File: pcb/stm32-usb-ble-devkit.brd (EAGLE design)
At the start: 90 x 50 mm, 98 parts, among them CN1 USB-MICROB-2TABS, CN2 USB-C-2.0-FEMALE, CN3 USB-C-2.0-FEMALE, Q2 AO3402, Q4 AO3401, Q6 AO3401, Q8 AO3401, U1 STM32F103-48LQFP, U2 STM32F205-64, U3 TUSB320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

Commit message: pcb: Fix STM32 VCAP pins
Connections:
- net GND: no longer U2.31, U2.47
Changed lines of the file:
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@@
 </signal>
 <signal name="GND">
-<contactref element="U1" pad="47"/>
 <contactref element="U1" pad="35"/>
 <contactref element="U1" pad="23"/>
@@
 <contactref element="C10" pad="1"/>
 <contactref element="R11" pad="1"/>
-<contactref element="U2" pad="47"/>
-<contactref element="U2" pad="31"/>
 <contactref element="C11" pad="1"/>
 <contactref element="C12" pad="1"/>

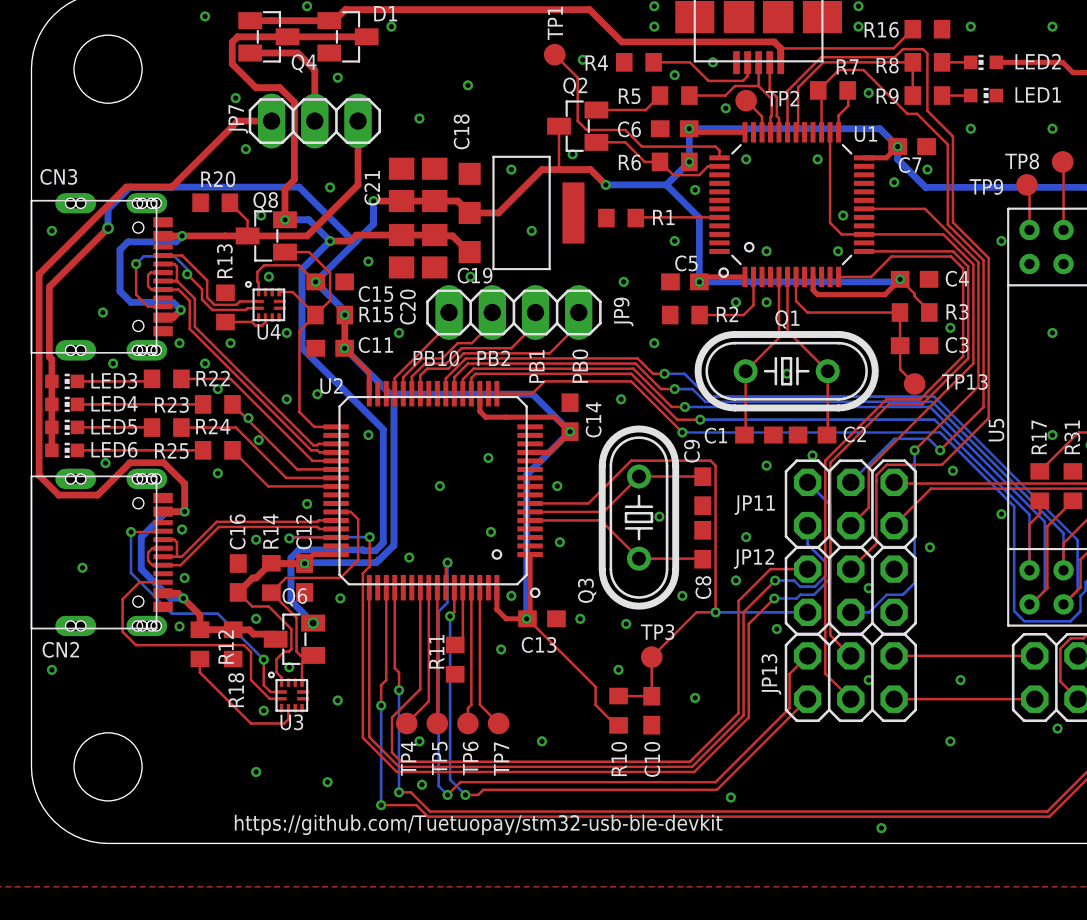
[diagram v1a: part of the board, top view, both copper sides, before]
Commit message: pcb: Misc changes following via size fix
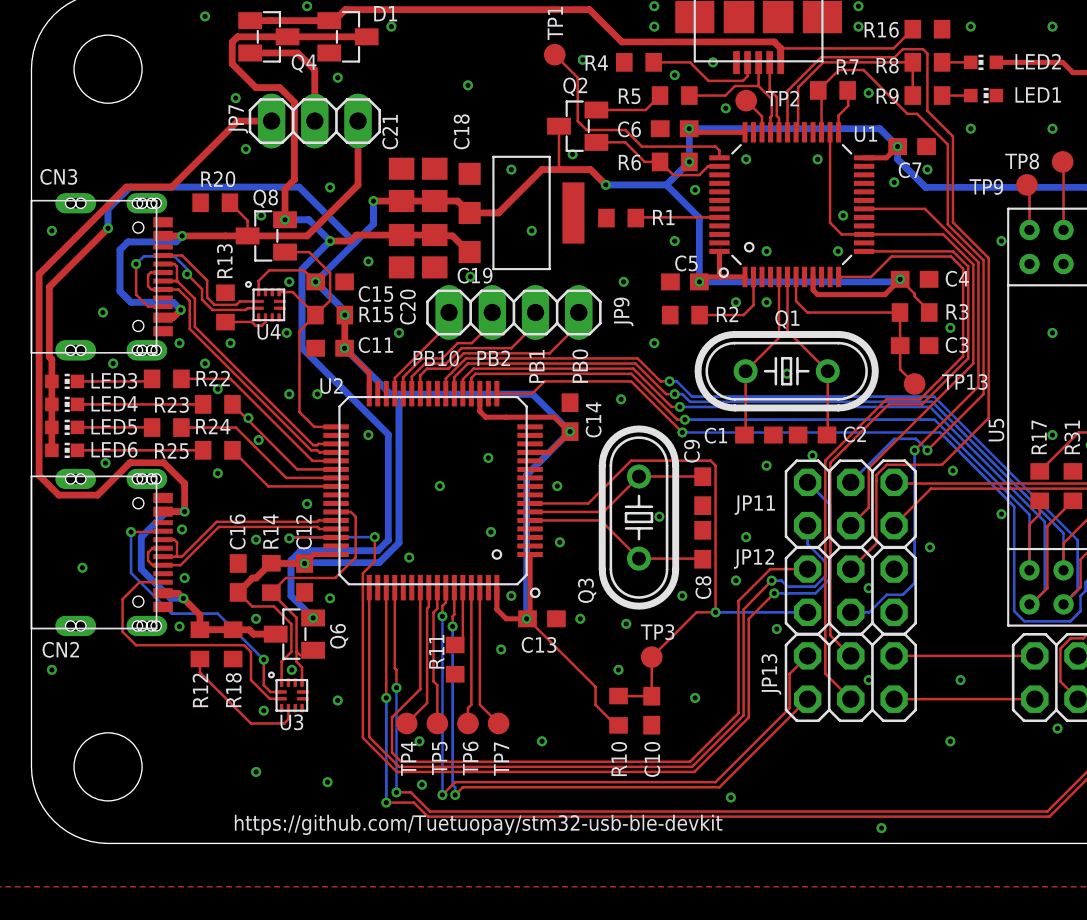
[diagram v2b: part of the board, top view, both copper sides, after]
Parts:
- moved Q6 0.30 mm to (15.4, 12.3)
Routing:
- net STM_TX: track 41.3 -> 38.3 mm
- net USB_FS_ID: track 16.8 -> 16.0 mm
- net STM_SWDIO: track 61.9 -> 62.5 mm
- net UART_STM2NRF: track 61.1 -> 60.6 mm

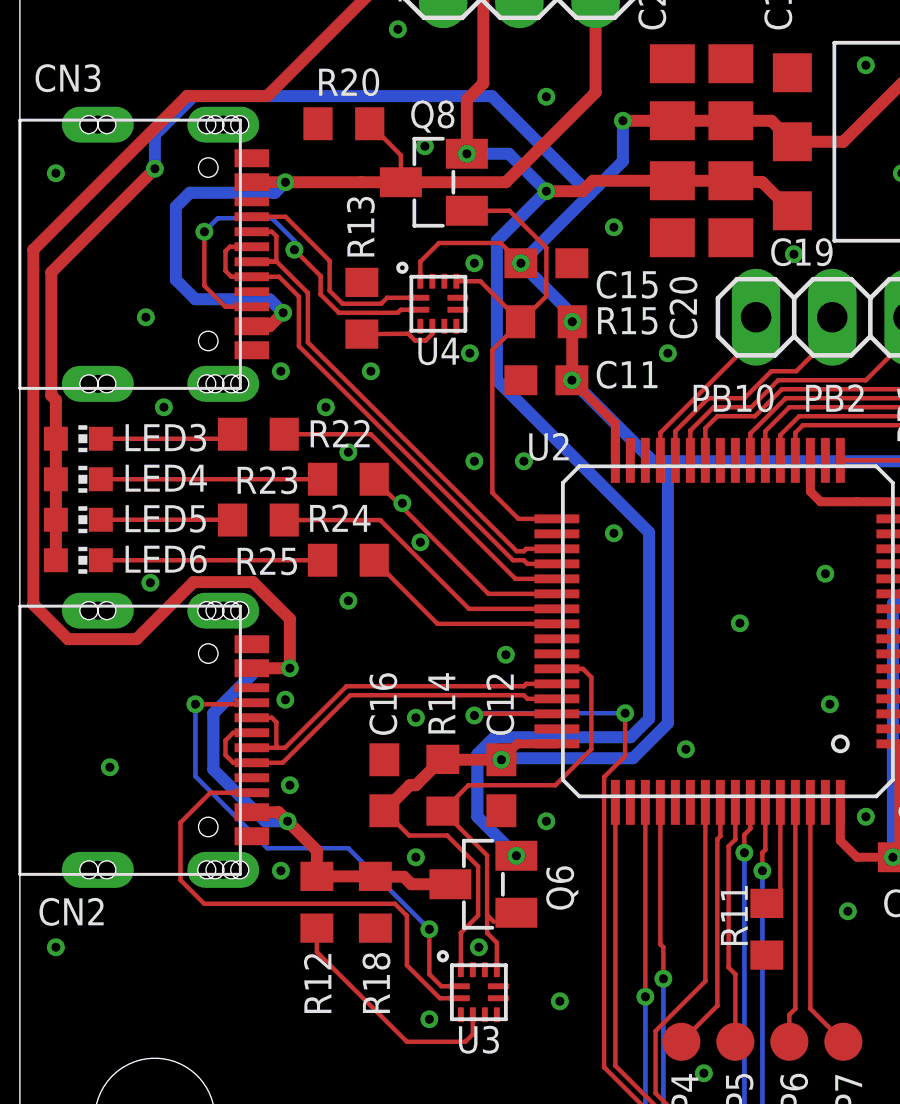
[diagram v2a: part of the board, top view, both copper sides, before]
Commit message: pcb: Add USB VBUS detection and USB BUS ON
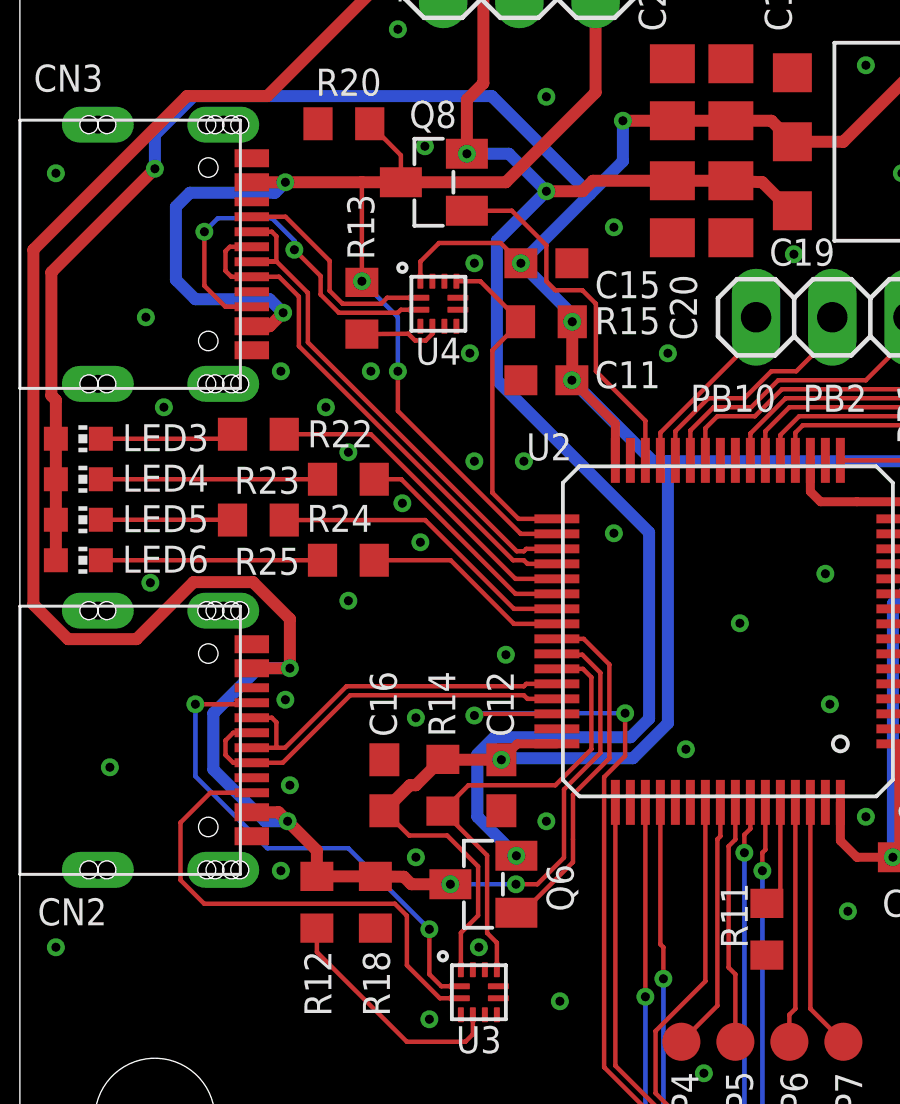
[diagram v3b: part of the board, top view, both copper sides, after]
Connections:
- new net USB_FS_ON: Q6.1, U2.41
- new net USB_HS_ON: Q8.1, U2.30
- net USB_FS_ID: no longer Q6.1
- net USB_FS_VBUS: now also U2.42
- net USB_HS_ID: no longer Q8.1
- net USB_HS_VBUS: now also U2.34
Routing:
- net USB_HS_VBUS: track 30.6 -> 45.7 mm, vias 2 -> 4
- net USB_FS_VBUS: track 57.7 -> 71.3 mm, vias 2 -> 4
- net USB_HS_ON: track 0.00 -> 12.2 mm
- net USB_FS_ON: track 0.00 -> 11.8 mm
- net USB_HS_ID: track 17.3 -> 11.3 mm
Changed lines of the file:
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@@
 <contactref element="U3" pad="9"/>
 <contactref element="R14" pad="2"/>
-<contactref element="Q6" pad="1"/>
-<wire x1="16.4" y1="11.05" x2="16.55" y2="11.05" width="0.15" layer="1"/>
-<wire x1="15.575" y1="11.275" x2="15.8" y2="11.05" width="0.15" layer="1"/>
 <wire x1="14.1" y1="14.7375" x2="14.95" y2="15.6" width="0.15" layer="1"/>
 <wire x1="17.85" y1="15.6" x2="19.05" y2="16.8" width="0.15" layer="1"/>
@@
 <contactref element="U4" pad="9"/>
 <contactref element="R15" pad="2"/>
-<contactref element="Q8" pad="1"/>
-<wire x1="17.55" y1="31.9" x2="16.6875" y2="31.05" width="0.15" layer="1"/>
-<wire x1="17.55" y1="33.5182" x2="17.55" y2="31.9" width="0.15" layer="1"/>
 <wire x1="14.55" y1="32.4" x2="15.35" y2="32.4" width="0.15" layer="1"/>
 <wire x1="15.35" y1="32.4" x2="16.6875" y2="31.05" width="0.15" layer="1"/>
-<wire x1="14.9" y1="34.75" x2="16.3182" y2="34.75" width="0.15" layer="1"/>
-<wire x1="16.3182" y1="34.75" x2="17.55" y2="33.5182" width="0.15" layer="1"/>
 <wire x1="16.6875" y1="31.05" x2="15.75" y2="30.1" width="0.15" layer="1"/>
 <wire x1="16.62" y1="24.48" x2="17.9" y2="24.48" width="0.15" layer="1"/>
@@
 <contactref element="U2" pad="38"/>
 <contactref element="R23" pad="1"/>
-<wire x1="17.9" y1="21.98" x2="15.62" y2="21.98" width="0.15" layer="1"/>
-<wire x1="15.62" y1="21.98" x2="11.8125" y2="25.8" width="0.15" layer="1"/>
+<wire x1="17.9" y1="21.98" x2="16.52" y2="21.98" width="0.15" layer="1"/>
+<wire x1="16.52" y1="21.98" x2="12.7125" y2="25.8" width="0.15" layer="1"/>
+<wire x1="12.7125" y1="25.8" x2="11.8125" y2="25.8" width="0.15" layer="1"/>
 </signal>
 <signal name="STM_LED2">
 <contactref element="U2" pad="39"/>
 <contactref element="R24" pad="1"/>
-<wire x1="8.8125" y1="24.44" x2="12.01" y2="24.44" width="0.15" layer="1"/>
-<wire x1="14.97" y1="21.48" x2="17.9" y2="21.48" width="0.15" layer="1"/>
-<wire x1="12.01" y1="24.44" x2="14.97" y2="21.48" width="0.15" layer="1"/>
+<wire x1="8.8125" y1="24.44" x2="13.51" y2="24.44" width="0.15" layer="1"/>
+<wire x1="16.47" y1="21.48" x2="17.9" y2="21.48" width="0.15" layer="1"/>
+<wire x1="13.51" y1="24.44" x2="16.47" y2="21.48" width="0.15" layer="1"/>
 </signal>
 <signal name="STM_LED3">
 <contactref element="U2" pad="40"/>
 <contactref element="R25" pad="1"/>
-<wire x1="17.9" y1="20.98" x2="13.92" y2="20.98" width="0.15" layer="1"/>
-<wire x1="13.92" y1="20.98" x2="11.8125" y2="23.1" width="0.15" layer="1"/>
+<wire x1="17.9" y1="20.98" x2="16.46823125" y2="20.98" width="0.15" layer="1"/>
+<wire x1="16.46823125" y1="20.98" x2="14.36073125" y2="23.1" width="0.15" layer="1"/>
+<wire x1="14.36073125" y1="23.1" x2="11.8125" y2="23.1" width="0.15" layer="1"/>
 </signal>
 <signal name="STM_DBG_TP_0">
@@
 <wire x1="7.73" y1="19.5" x2="9" y2="19.5" width="0.4" layer="1"/>
 <wire x1="8.925" y1="14.4" x2="8.175" y2="14.4" width="0.4" layer="16"/>
+<contactref element="U2" pad="42"/>
+<wire x1="17.9" y1="19.98" x2="17.93" y2="19.95" width="0.15" layer="1"/>
+<wire x1="17.93" y1="19.95" x2="18.75" y2="19.95" width="0.15" layer="1"/>
+<wire x1="18.75" y1="19.95" x2="19.35" y2="19.35" width="0.15" layer="1"/>
+<wire x1="19.35" y1="16.67573125" x2="18.137134375" y2="15.462865625" width="0.15" layer="1"/>
+<wire x1="19.35" y1="19.35" x2="19.35" y2="16.67573125" width="0.15" layer="1"/>
+<wire x1="18.137134375" y1="15.462865625" x2="18.137134375" y2="13.187134375" width="0.15" layer="1"/>
+<wire x1="18.137134375" y1="13.187134375" x2="17.25" y2="12.3" width="0.15" layer="1"/>
+<wire x1="17.25" y1="12.3" x2="16.53639375" y2="12.3" width="0.15" layer="1"/>
+<via x="16.53639375" y="12.3" extent="1-16" drill="0.3" diameter="0.6"/>
+<wire x1="16.53639375" y1="12.3" x2="14.35" y2="12.3" width="0.15" layer="16"/>
+<via x="14.35" y="12.3" extent="1-16" drill="0.3" diameter="0.6"/>
+<wire x1="7.95" y1="19.5" x2="9" y2="19.5" width="0.4" layer="16"/>
 </signal>
 <signal name="USB_HS_VBUS_DET">
@@
 <wire x1="7.73" y1="35.7" x2="8.85" y2="35.7" width="0.4" layer="1"/>
 <wire x1="11.4" y1="32.3625" x2="11.4" y2="32.4" width="0.15" layer="1"/>
+<contactref element="U2" pad="34"/>
+<wire x1="11.4" y1="32.4" x2="11.4" y2="35.7" width="0.15" layer="1"/>
+<wire x1="17.9" y1="23.98" x2="16.69573125" y2="23.98" width="0.15" layer="1"/>
+<wire x1="12.6" y1="28.07573125" x2="12.6" y2="29.4" width="0.15" layer="1"/>
+<via x="12.6" y="29.4" extent="1-16" drill="0.3" diameter="0.6"/>
+<wire x1="12.6" y1="29.4" x2="12.6" y2="31.2" width="0.15" layer="16"/>
+<wire x1="12.6" y1="31.2" x2="11.4" y2="32.4" width="0.15" layer="16"/>
+<via x="11.4" y="32.4" extent="1-16" drill="0.3" diameter="0.6"/>
+<wire x1="16.69573125" y1="23.98" x2="12.6" y2="28.07573125" width="0.15" layer="1"/>
 </signal>
 <signal name="USB_FS_CC1">
@@
 <wire x1="63.85" y1="17.25" x2="62.65" y2="16.05" width="0.15" layer="1"/>
 </signal>
+<signal name="USB_FS_ON">
+<contactref element="U2" pad="41"/>
+<contactref element="Q6" pad="1"/>
+<wire x1="18.79426875" y1="20.48" x2="19.65" y2="19.62426875" width="0.15" layer="1"/>
+<wire x1="19.65" y1="16.4982" x2="18.43714375" y2="15.28534375" width="0.15" layer="1"/>
+<wire x1="18.43714375" y1="15.28534375" x2="18.43714375" y2="13.8" width="0.15" layer="1"/>
+<wire x1="19.65" y1="19.62426875" x2="19.65" y2="16.4982" width="0.15" layer="1"/>
+<wire x1="18.43714375" y1="13.8" x2="18.43714375" y2="13.8" width="0.15" layer="1"/>
+<wire x1="18.43714375" y1="13.03714375" x2="18.43714375" y2="13.8" width="0.15" layer="1"/>
+<wire x1="16.55" y1="11.35" x2="16.75" y2="11.35" width="0.15" layer="1"/>
+<wire x1="16.75" y1="11.35" x2="18.43714375" y2="13.03714375" width="0.15" layer="1"/>
+<wire x1="17.9" y1="20.48" x2="18.79426875" y2="20.48" width="0.15" layer="1"/>
+</signal>
+<signal name="USB_HS_ON">
+<contactref element="U2" pad="30"/>
+<contactref element="Q8" pad="1"/>
+<wire x1="20.85" y1="26.43" x2="20.85" y2="27.75" width="0.15" layer="1"/>
+<wire x1="20.85" y1="27.75" x2="19.2" y2="29.4" width="0.15" layer="1"/>
+<wire x1="19.2" y1="31.65" x2="18.75" y2="32.1" width="0.15" layer="1"/>
+<wire x1="17.85" y1="32.1" x2="17.55" y2="32.4" width="0.15" layer="1"/>
+<wire x1="16.4" y1="34.75" x2="14.9" y2="34.75" width="0.15" layer="1"/>
+<wire x1="19.2" y1="29.4" x2="19.2" y2="31.65" width="0.15" layer="1"/>
+<wire x1="18.75" y1="32.1" x2="17.85" y2="32.1" width="0.15" layer="1"/>
+<wire x1="17.55" y1="32.4" x2="17.55" y2="33.6" width="0.15" layer="1"/>
+<wire x1="17.55" y1="33.6" x2="16.4" y2="34.75" width="0.15" layer="1"/>
+</signal>
 </signals>

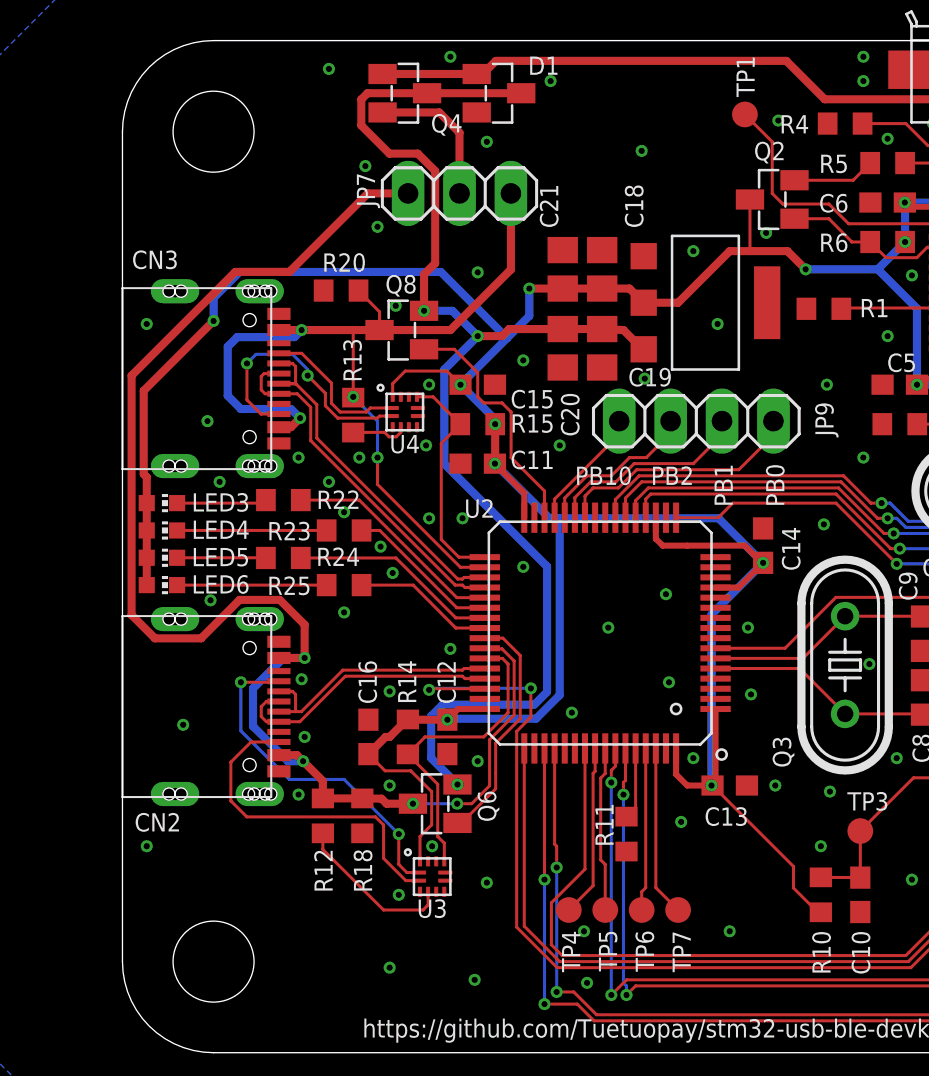
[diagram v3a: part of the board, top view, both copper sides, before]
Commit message: pcb: Increased space between USB-C connectors
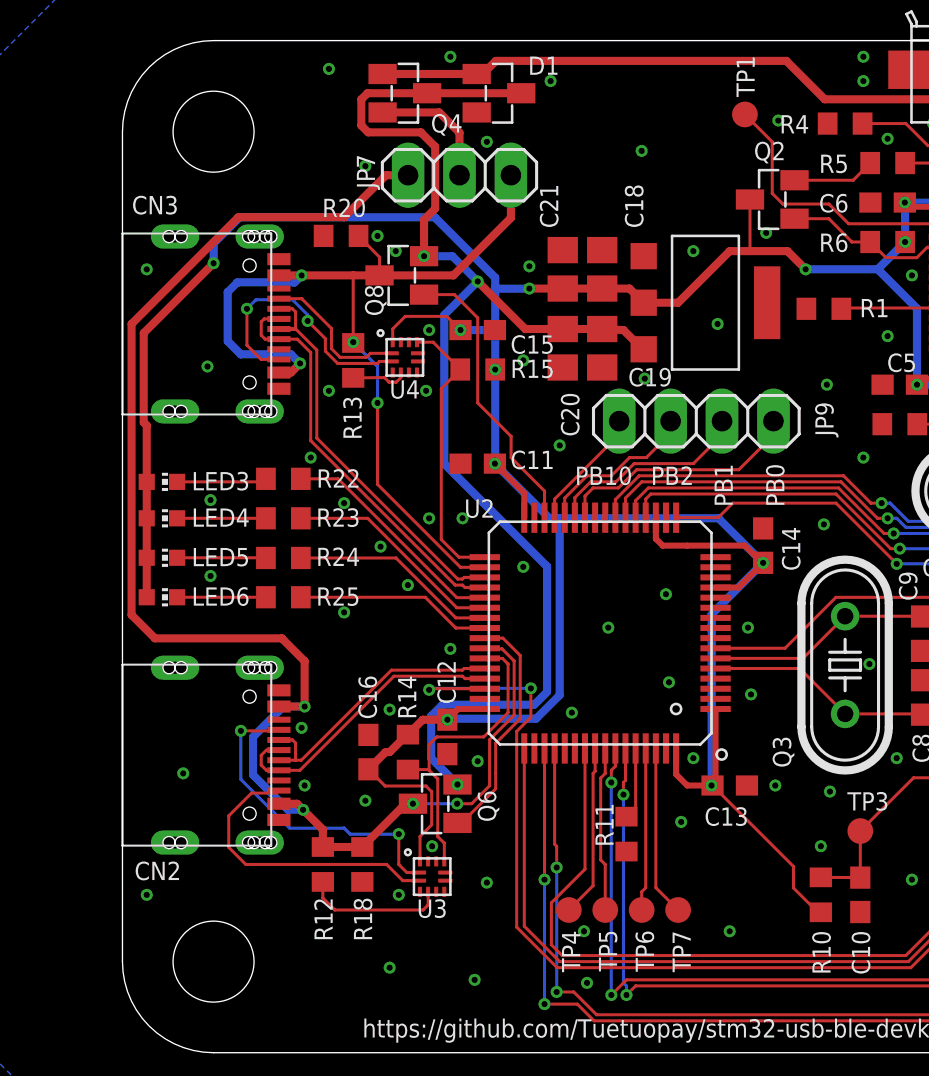
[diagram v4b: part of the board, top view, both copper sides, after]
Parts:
- moved R25 3.06 mm to (7.95, 22.5)
- moved R23 3.06 mm to (7.95, 26.4)
- moved C15 2.70 mm to (17.6, 35.7)
- moved CN3 2.70 mm to (0.00, 36.0)
- moved R13 2.70 mm to (11.4, 34.2)
- moved R20 2.70 mm to (10.8, 40.4)
- moved U4 2.70 mm to (13.9, 34.4)
- moved R15 2.70 mm to (17.6, 33.8)
- moved Q8 2.70 mm to (13.8, 38.4)
- moved CN2 2.40 mm to (0.00, 14.7)
- moved R12 2.40 mm to (9.90, 9.30)
- moved R18 2.40 mm to (11.8, 9.30)
- moved LED3 1.05 mm to (1.95, 28.2)
- moved R22 1.05 mm to (7.95, 28.4)
- moved JP7 0.90 mm to (16.6, 43.4)
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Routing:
- net +3V3: track 270.4 -> 274.8 mm
- net STM_LED1: track 7.67 -> 10.9 mm
- net STM_LEDR3: track 7.39 -> 4.39 mm
- net STM_LEDR1: track 7.39 -> 4.39 mm
- net STM_LED3: track 6.97 -> 9.72 mm
- net USB_HS_N: track 17.2 -> 19.9 mm
- net USB_HS_ID: track 11.3 -> 14.0 mm
- net USB_HS_P: track 17.7 -> 20.4 mm
- net USB_FS_VBUS: track 71.3 -> 73.8 mm
- net USB_HS_ON: track 12.2 -> 14.4 mm
- net USB_FS_CC2: track 16.6 -> 14.6 mm
- net +5V: track 63.4 -> 65.0 mm
- net USB_FS_N: track 12.8 -> 13.8 mm
- net USB_FS_CC1: track 16.9 -> 15.9 mm
- net USB_FS_P: track 13.6 -> 14.6 mm
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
